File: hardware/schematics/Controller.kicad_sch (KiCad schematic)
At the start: 24 parts, among them U2 MAX17048, U3 IP5306/FM5324UI, U6 SSD1306, U7 Battery

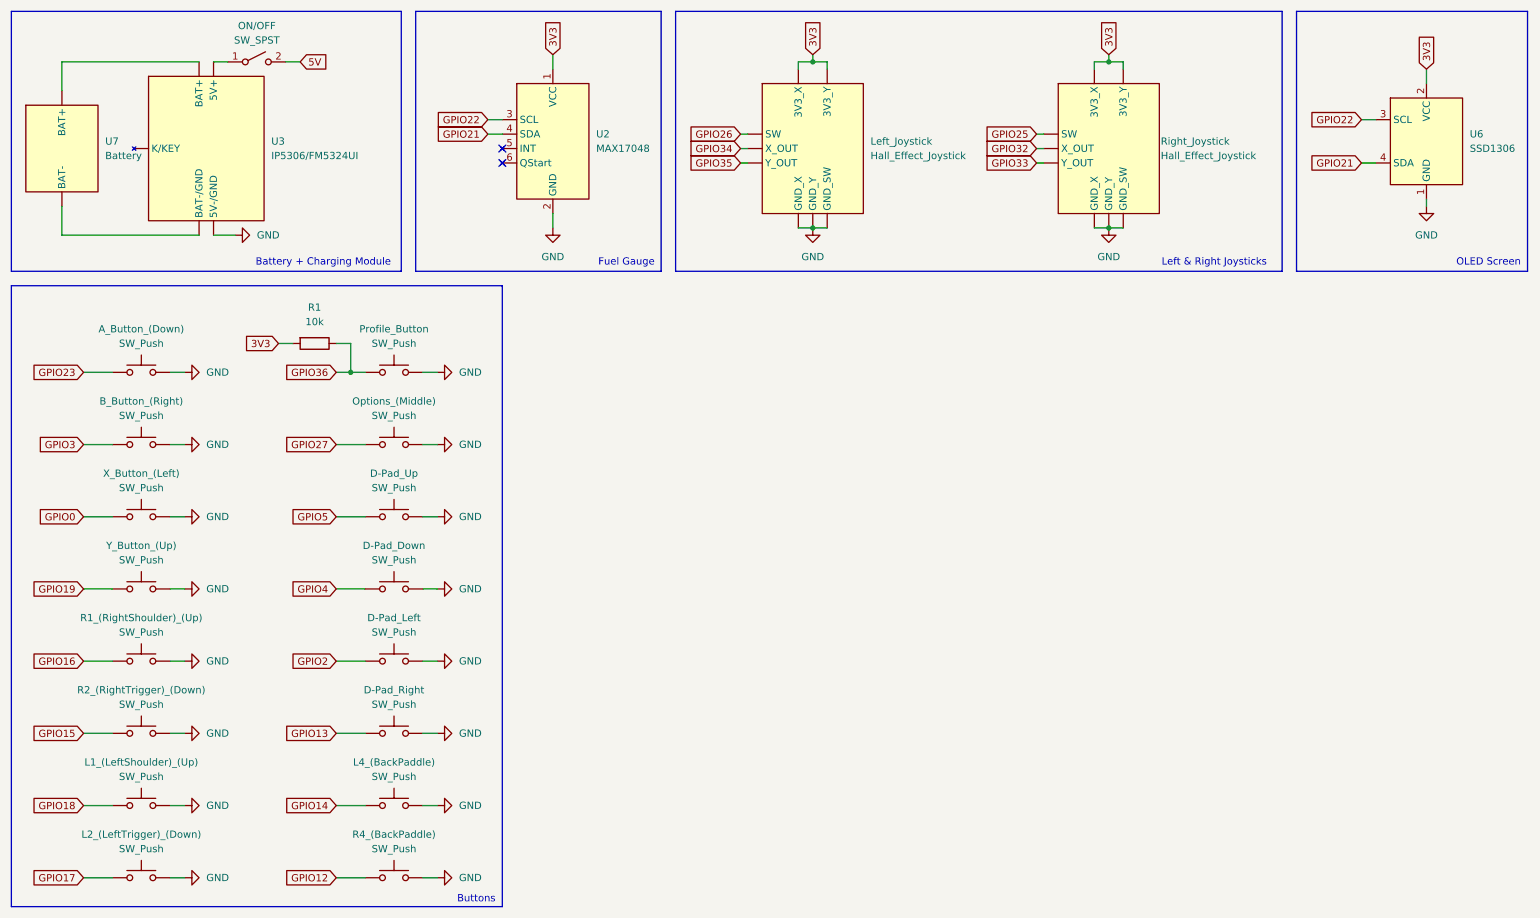
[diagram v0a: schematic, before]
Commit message: Finalize hardware wiring, pinouts, and test firmware
- Complete physical wiring, component assembly, and enclosure fit adjustments.
- Update pin assignments (swap L3/R3, reassign GPIO3 to GPIO39 with a 10 kΩ pull-up).
- Add 1 kΩ pull-up resistor to GPIO2 to resolve constant-press hardware issue.
- Add dedicated PlatformIO test firmware to validate buttons and analog axes.
- Update electrical schematics, pinout documentation, and diagrams.
- Add media files (images and video) demonstrating wiring, placement, and firmware test.
- Document progress and findings in DevelopmentLog.md.
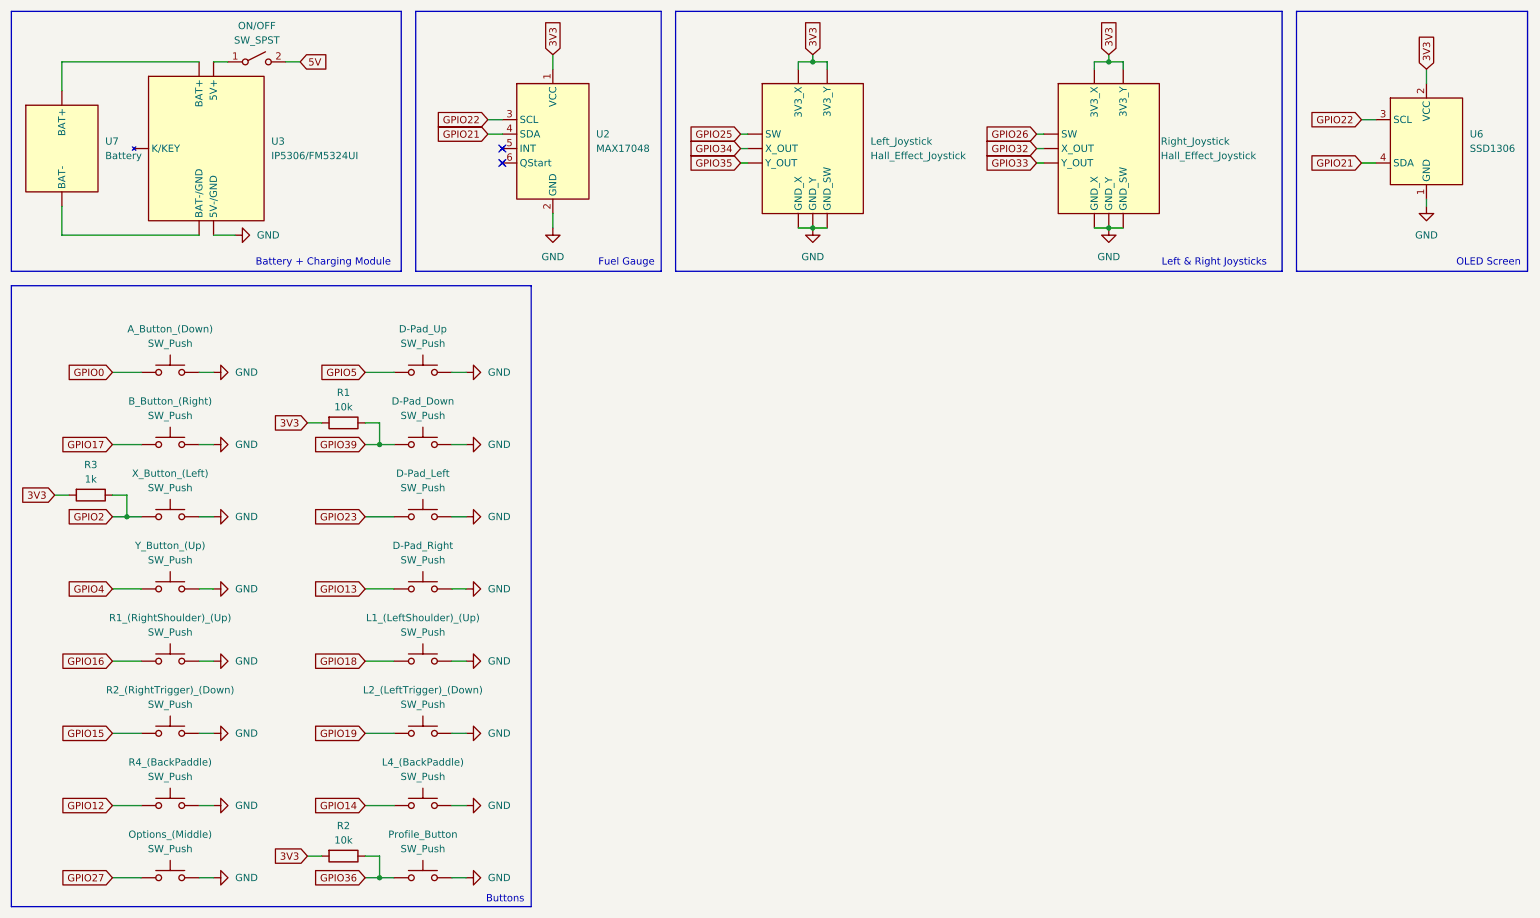
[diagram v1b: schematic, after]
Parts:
- added R1: 10k, symbol Device:R
- added R3: 1k, symbol Device:R
- renumbered R1 to R2
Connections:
- net GPIO3 is gone; now on net GPIO17: B_Button_(Right).1
- net 3V3: now also R1.2, R3.2
- net GPIO0: now also A_Button_(Down).1; no longer X_Button_(Left).1
- net GPIO17: no longer L2_(LeftTrigger)_(Down).1
- net GPIO19: now also L2_(LeftTrigger)_(Down).1; no longer Y_Button_(Up).1
- net GPIO2: now also X_Button_(Left).1, R3.1; no longer D-Pad_Left.1
- net GPIO23: now also D-Pad_Left.1; no longer A_Button_(Down).1
- net GPIO25: now also Left_Joystick. (Y_OUT); no longer Right_Joystick. (Y_OUT)
- net GPIO26: now also Right_Joystick. (Y_OUT); no longer Left_Joystick. (Y_OUT)
- net GPIO4: now also Y_Button_(Up).1; no longer D-Pad_Down.1
- new net: U3. (K/KEY), U7. (BAT-)
- new net GPIO39: D-Pad_Down.1, R1.1
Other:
- moved on the sheet: D-Pad_Right, D-Pad_Up, L1_(LeftShoulder)_(Up), L4_(BackPaddle), Options_(Middle), Profile_Button, R1_(RightShoulder)_(Up), R2, R2_(RightTrigger)_(Down), R4_(BackPaddle), Y_Button_(Up)
